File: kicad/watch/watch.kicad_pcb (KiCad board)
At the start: 2 copper layers, 35.6 x 25.4 mm, 55 parts, among them IC1 113990582, J1 USB_C_Receptacle_USB2.0, J2 Conn_01x04_Female, J3 Conn_01x04_Female, J4 Memory LCD, J5 LCD Frontlight, J6 Buzzer, Q1 DMN6140L, Q2 DMN6140L, SW1 SW_Push, SW2 SW_Push, U1 W25X20CLUXIG, U2 MCP73831-2-OT, U3 M41T62Q, U4 TPS63001, Y1 Crystal, Y2 32.768 kHz

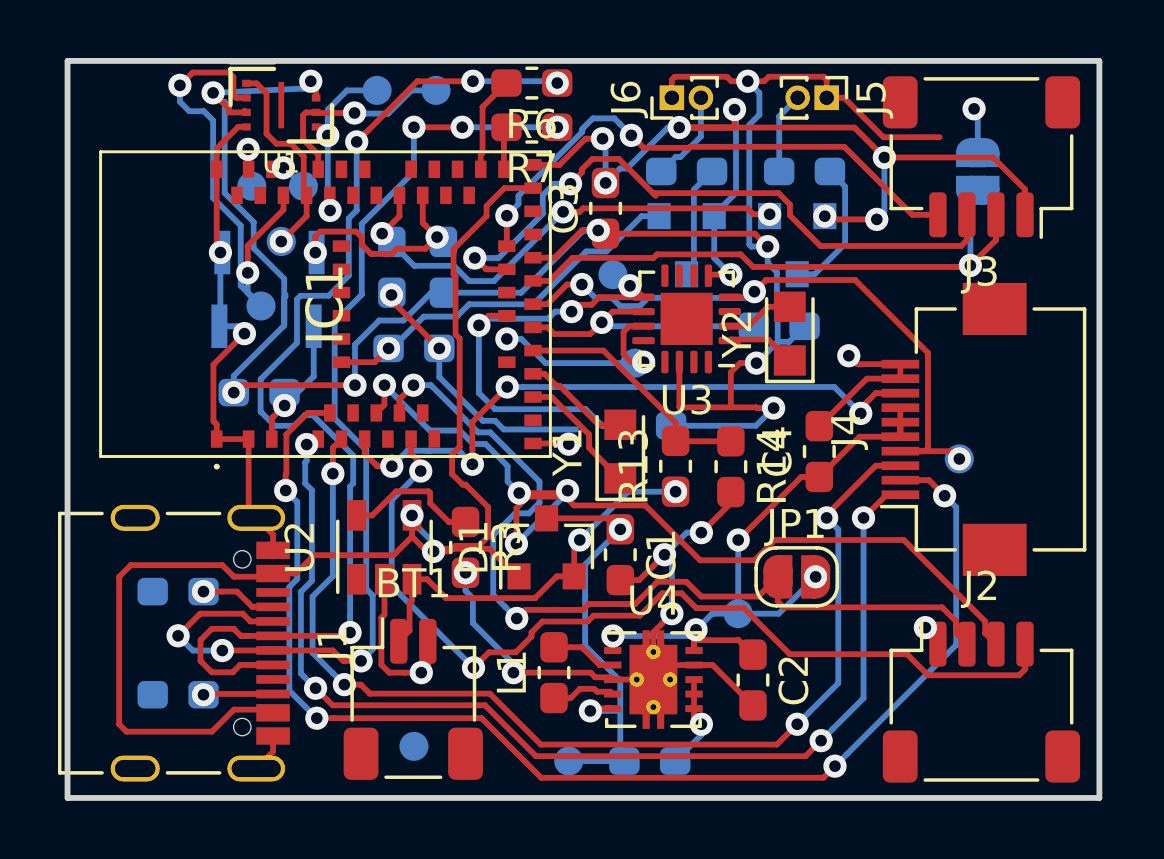
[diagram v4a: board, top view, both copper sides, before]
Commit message: add button panel, finish silk for main pcb
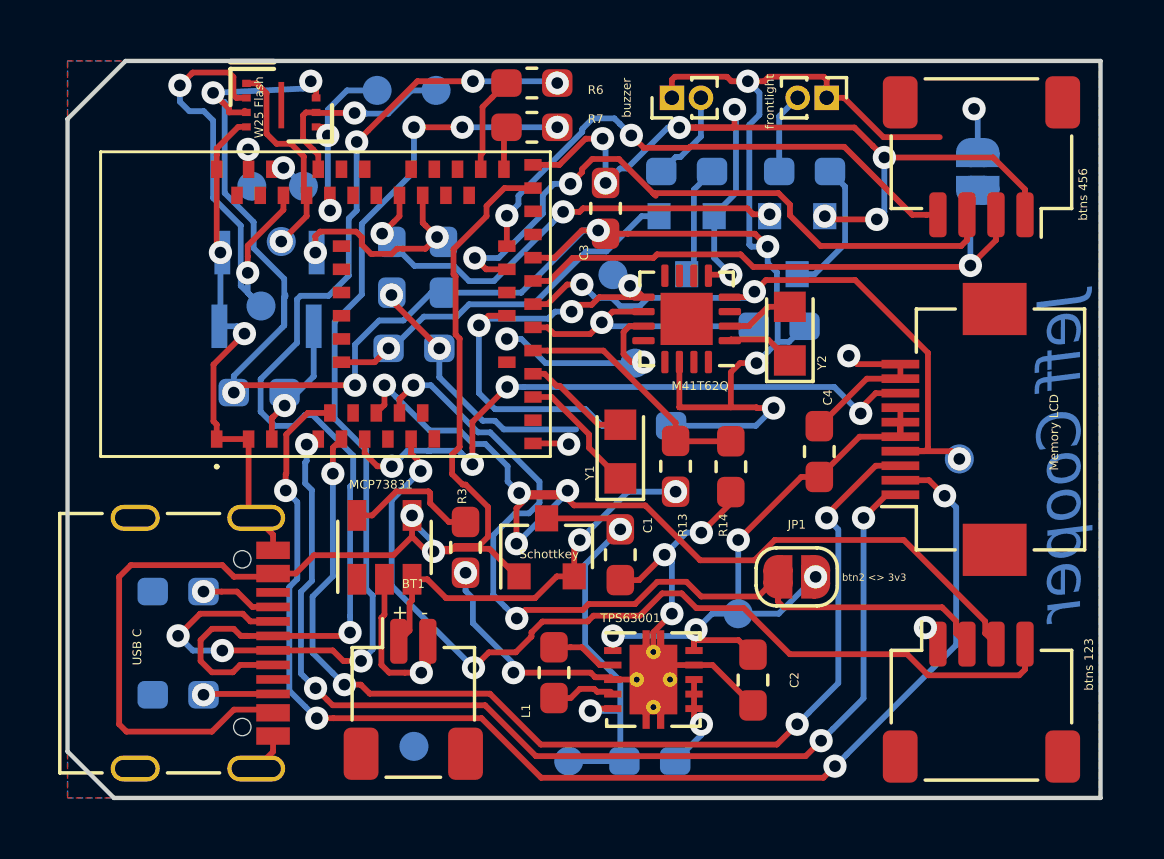
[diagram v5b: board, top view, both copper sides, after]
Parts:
- removed TP6: TestPoint, TestPoint:TestPoint_Pad_D1.0mm
- added SDA: TestPoint, TestPoint:TestPoint_Pad_D1.0mm, B.Cu at (18.8, 7.37)
- 3v3 <> btn6: renamed from JP2
- Memory LCD: renamed from J4
- USB C: renamed from J1
- W25 Flash: renamed from U1
- btns 123: renamed from J2
- btns 456: renamed from J3
- renumbered TP1 to 3v3, SW2 to BOOT, TP10 to FLASH_CLK, TP11 to FLASH_CS, TP9 to FLASH_DI, TP12 to FLASH_DO, TP2 to GND, U3 to M41T62Q, U2 to MCP73831, SW1 to RESET, TP8 to RTC_IRQ, TP5 to SCL, TP7 to SQW, TP3 to SWDCLK, TP4 to SWDIO, D1 to Schottkey, U4 to TPS63001, TP13 to VIN, J6 to buzzer, J5 to frontlight
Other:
- outline, holes or cut-outs redrawn
- board text added: "+ -"
- board text added: "Jeff Cooper"
- board text added: "btn2 <> 3v3"
- board text added: "jeff@thejeffcooper.com Proudly designed in Pittsburgh, PA"
- board text added: "nrf52 watch mk 1 rev 1"
